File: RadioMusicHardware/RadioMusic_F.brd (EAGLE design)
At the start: 107 x 19 mm, 31 parts, among them X1 VERT_SD_CARD

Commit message: Fixed issues on Rev1 proto boards
Diodes changed to BAT42
LED resistors changed to 2k
Ground error on Front board fixed
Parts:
- D7, D8: value BAT81 -> BAT42
- R11, R12, R13, R14, R15: value 1k -> 2K
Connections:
- removed net GND: R10.1, R21.1
- net GND_F: now also R10.1, R21.1
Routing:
- net GND: track 5.93 -> 0.00 mm
- net GND_F: track 172.3 -> 174.2 mm
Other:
- board text added: "<-BAT42 x2"
- board text removed: "<-BAT81 x2"
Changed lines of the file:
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@@
 <text x="70.485" y="11.43" size="1.27" layer="22" rot="MR90">--&gt;</text>
 <text x="71.755" y="6.985" size="1.27" layer="22" rot="SMR270">--&gt;</text>
-<text x="36.3474" y="13.9192" size="0.762" layer="21" rot="R90" align="center-left">&lt;-BAT81
+<text x="36.3474" y="13.9192" size="0.762" layer="21" rot="R90" align="center-left">&lt;-BAT42
    x2</text>
 <text x="74.0664" y="0.7112" size="0.762" layer="21" distance="40">Be super careful with
@@
 <element name="R20" library="TomW" package="0207/10" value="100k" x="76.835" y="9.525" rot="R90"/>
 <element name="R21" library="TomW" package="0207/10" value="200k" x="79.375" y="9.525" rot="R90"/>
-<element name="D7" library="diode" package="DO34-7" value="BAT81" x="36.83" y="9.525" smashed="yes" rot="R90"/>
-<element name="D8" library="diode" package="DO34-7" value="BAT81" x="34.925" y="9.525" smashed="yes" rot="R270"/>
+<element name="D7" library="diode" package="DO34-7" value="BAT42" x="36.83" y="9.525" smashed="yes" rot="R90"/>
+<element name="D8" library="diode" package="DO34-7" value="BAT42" x="34.925" y="9.525" smashed="yes" rot="R270"/>
 <element name="R19" library="TomW" package="0207/10" value="100k" x="32.385" y="9.525" rot="R90"/>
 <element name="R18" library="TomW" package="0207/10" value="220R" x="29.845" y="9.525" rot="R90"/>
@@
 <element name="LED3" library="TomW" package="LED3MM" value="" x="105.156" y="7.366" rot="R270"/>
 <element name="LED4" library="TomW" package="LED3MM" value="" x="105.156" y="2.921" rot="R270"/>
-<element name="R11" library="TomW" package="0207/10" value="1k" x="97.155" y="17.145"/>
-<element name="R12" library="TomW" package="0207/10" value="1k" x="102.235" y="9.525" rot="R90"/>
-<element name="R13" library="TomW" package="0207/10" value="1k" x="81.915" y="9.525" rot="R90"/>
-<element name="R14" library="TomW" package="0207/10" value="1k" x="95.885" y="1.905"/>
+<element name="R11" library="TomW" package="0207/10" value="2K" x="97.155" y="17.145"/>
+<element name="R12" library="TomW" package="0207/10" value="2K" x="102.235" y="9.525" rot="R90"/>
+<element name="R13" library="TomW" package="0207/10" value="2K" x="81.915" y="9.525" rot="R90"/>
+<element name="R14" library="TomW" package="0207/10" value="2K" x="95.885" y="1.905"/>
 <element name="X1" library="TomW" package="VERT_MICROSD" value="VERT_SD_CARD" x="44.45" y="16.51"/>
 <element name="LED5" library="TomW" package="LED3MM" value="" x="52.705" y="3.175" smashed="yes" rot="R270">
 <attribute name="VALUE" x="51.054" y="1.27" size="1.27" layer="51" ratio="10" rot="R270"/>
 </element>
-<element name="R15" library="TomW" package="0207/10" value="1k" x="55.245" y="9.525" rot="R90"/>
+<element name="R15" library="TomW" package="0207/10" value="2K" x="55.245" y="9.525" rot="R90"/>
 <element name="JP2" library="SparkFun-Connectors" package="1X11_LOCK" value="M11LOCK" x="82.55" y="17.145" locked="yes" smashed="yes" rot="MR0"/>
 <element name="JP4" library="SparkFun-Connectors" package="1X07_LOCK" value="" x="57.15" y="1.27" locked="yes" smashed="yes" rot="MR180">
@@
 </elements>
 <signals>
-<signal name="GND" class="2" airwireshidden="yes">
-<contactref element="R10" pad="1"/>
-<contactref element="R21" pad="1"/>
-<wire x1="80.4672" y1="5.4864" x2="79.4512" y2="4.4704" width="0.4572" layer="1"/>
-<wire x1="83.312" y1="5.4864" x2="80.4672" y2="5.4864" width="0.4572" layer="1"/>
-<wire x1="84.328" y1="4.4704" x2="83.312" y2="5.4864" width="0.4572" layer="1"/>
-<wire x1="79.4512" y1="4.4704" x2="79.375" y2="4.445" width="0.4572" layer="1"/>
-<wire x1="84.328" y1="4.4704" x2="84.455" y2="4.445" width="0.4572" layer="1"/>
-</signal>
 <signal name="VBAT">
 </signal>
@@
 <wire x1="88.1888" y1="6.9088" x2="88.25" y2="7.025" width="0.3048" layer="16"/>
 </signal>
-<signal name="GND_F" class="2" airwireshidden="yes">
+<signal name="GND_F" class="2">
 <contactref element="X1" pad="P$6"/>
 <contactref element="X1" pad="GND1"/>
@@
 <wire x1="40.0304" y1="13.208" x2="40.15" y2="13.34" width="0.4572" layer="16"/>
 <wire x1="34.9504" y1="5.8928" x2="34.925" y2="5.715" width="0.4572" layer="16"/>
-<wire x1="89.2048" y1="3.4544" x2="89.7128" y2="2.9464" width="0.4572" layer="1"/>
-<wire x1="89.7128" y1="2.9464" x2="90.6272" y2="2.032" width="0.4572" layer="1"/>
-<wire x1="82.9056" y1="3.4544" x2="89.2048" y2="3.4544" width="0.4572" layer="1"/>
-<wire x1="81.915" y1="4.445" x2="82.9056" y2="3.4544" width="0.4572" layer="1"/>
-<wire x1="90.6272" y1="2.032" x2="90.805" y2="1.905" width="0.4572" layer="1"/>
 <wire x1="100.9904" y1="3.048" x2="102.2096" y2="4.2672" width="0.4572" layer="1"/>
-<wire x1="89.8144" y1="3.048" x2="100.9904" y2="3.048" width="0.4572" layer="1"/>
 <wire x1="102.2096" y1="4.2672" x2="102.235" y2="4.445" width="0.4572" layer="1"/>
-<wire x1="89.8144" y1="3.048" x2="89.7128" y2="2.9464" width="0.4572" layer="1"/>
 <wire x1="88.392" y1="13.4112" x2="89.5096" y2="14.5288" width="0.4572" layer="16"/>
 <wire x1="89.5096" y1="14.5288" x2="92.0496" y2="17.0688" width="0.4572" layer="16"/>
@@
 <wire x1="60.1472" y1="12.192" x2="60.31" y2="12.025" width="0.4572" layer="1"/>
 <via x="57.5056" y="12.192" extent="1-16" drill="0.3048"/>
+<contactref element="R10" pad="1"/>
+<contactref element="R21" pad="1"/>
+<wire x1="100.9904" y1="3.048" x2="91.948" y2="3.048" width="0.4572" layer="1"/>
+<wire x1="91.948" y1="3.048" x2="90.805" y2="1.905" width="0.4572" layer="1"/>
+<wire x1="79.375" y1="4.445" x2="81.915" y2="4.445" width="0.4572" layer="1"/>
+<wire x1="81.915" y1="4.445" x2="84.455" y2="4.445" width="0.4572" layer="1"/>
+<wire x1="84.455" y1="4.445" x2="88.265" y2="4.445" width="0.4572" layer="1"/>
+<wire x1="88.265" y1="4.445" x2="90.805" y2="1.905" width="0.4572" layer="1"/>
 </signal>
 <signal name="CHANNEL_CV_F">

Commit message: Change resistor values to reduce CV noise
Fixes #13
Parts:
- R10, R21: value 200k -> 47k
- R11, R12, R13, R14, R15: value 2K -> 1.5k
- R20, R9: value 100k -> 22k
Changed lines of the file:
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@@
 <attribute name="NAME" x="6.35" y="1.3208" size="1.016" layer="21" rot="R180"/>
 </element>
-<element name="R9" library="TomW" package="0207/10" value="100k" x="57.785" y="9.525" rot="R90"/>
-<element name="R10" library="TomW" package="0207/10" value="200k" x="84.455" y="9.525" rot="R90"/>
+<element name="R9" library="TomW" package="0207/10" value="22k" x="57.785" y="9.525" rot="R90"/>
+<element name="R10" library="TomW" package="0207/10" value="47k" x="84.455" y="9.525" rot="R90"/>
 <element name="R17" library="TomW" package="0207/10" value="220R" x="74.295" y="9.525" rot="R90"/>
 <element name="TIME-POT" library="TomW" package="EVUF" value="50k" x="67.31" y="9.525" smashed="yes" rot="R270">
@@
 <attribute name="NAME" x="21.3614" y="11.2776" size="1.016" layer="21" rot="R180"/>
 </element>
-<element name="R20" library="TomW" package="0207/10" value="100k" x="76.835" y="9.525" rot="R90"/>
-<element name="R21" library="TomW" package="0207/10" value="200k" x="79.375" y="9.525" rot="R90"/>
+<element name="R20" library="TomW" package="0207/10" value="22k" x="76.835" y="9.525" rot="R90"/>
+<element name="R21" library="TomW" package="0207/10" value="47k" x="79.375" y="9.525" rot="R90"/>
 <element name="D7" library="diode" package="DO34-7" value="BAT42" x="36.83" y="9.525" smashed="yes" rot="R90"/>
 <element name="D8" library="diode" package="DO34-7" value="BAT42" x="34.925" y="9.525" smashed="yes" rot="R270"/>
@@
 <element name="LED3" library="TomW" package="LED3MM" value="" x="105.156" y="7.366" rot="R270"/>
 <element name="LED4" library="TomW" package="LED3MM" value="" x="105.156" y="2.921" rot="R270"/>
-<element name="R11" library="TomW" package="0207/10" value="2K" x="97.155" y="17.145"/>
-<element name="R12" library="TomW" package="0207/10" value="2K" x="102.235" y="9.525" rot="R90"/>
-<element name="R13" library="TomW" package="0207/10" value="2K" x="81.915" y="9.525" rot="R90"/>
-<element name="R14" library="TomW" package="0207/10" value="2K" x="95.885" y="1.905"/>
+<element name="R11" library="TomW" package="0207/10" value="1.5k" x="97.155" y="17.145"/>
+<element name="R12" library="TomW" package="0207/10" value="1.5k" x="102.235" y="9.525" rot="R90"/>
+<element name="R13" library="TomW" package="0207/10" value="1.5k" x="81.915" y="9.525" rot="R90"/>
+<element name="R14" library="TomW" package="0207/10" value="1.5k" x="95.885" y="1.905"/>
 <element name="X1" library="TomW" package="VERT_MICROSD" value="VERT_SD_CARD" x="44.45" y="16.51"/>
 <element name="LED5" library="TomW" package="LED3MM" value="" x="52.705" y="3.175" smashed="yes" rot="R270">
 <attribute name="VALUE" x="51.054" y="1.27" size="1.27" layer="51" ratio="10" rot="R270"/>
 </element>
-<element name="R15" library="TomW" package="0207/10" value="2K" x="55.245" y="9.525" rot="R90"/>
+<element name="R15" library="TomW" package="0207/10" value="1.5k" x="55.245" y="9.525" rot="R90"/>
 <element name="JP2" library="SparkFun-Connectors" package="1X11_LOCK" value="M11LOCK" x="82.55" y="17.145" locked="yes" smashed="yes" rot="MR0"/>
 <element name="JP4" library="SparkFun-Connectors" package="1X07_LOCK" value="" x="57.15" y="1.27" locked="yes" smashed="yes" rot="MR180">

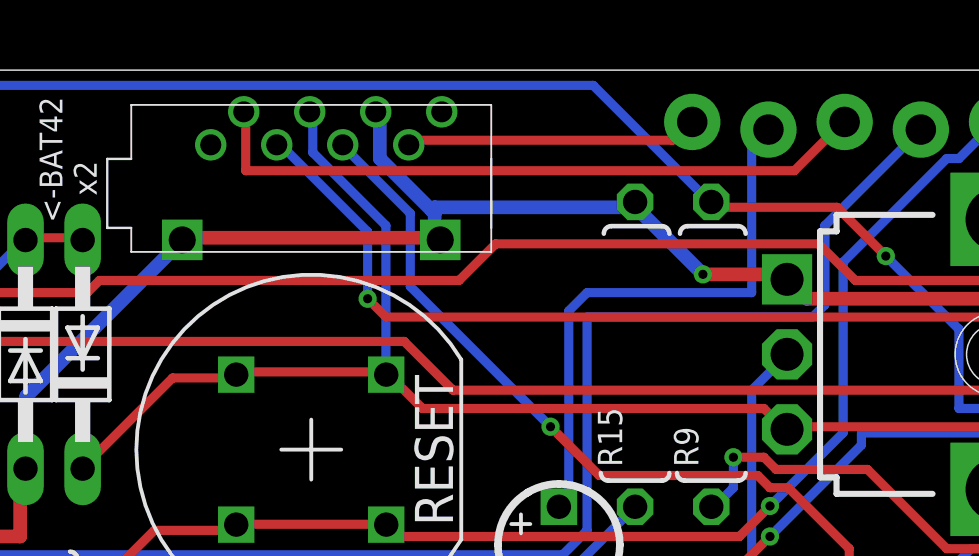
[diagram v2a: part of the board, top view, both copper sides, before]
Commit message: Fix SD Card pin position
Pin holes were 0.5mm off Fixes #14
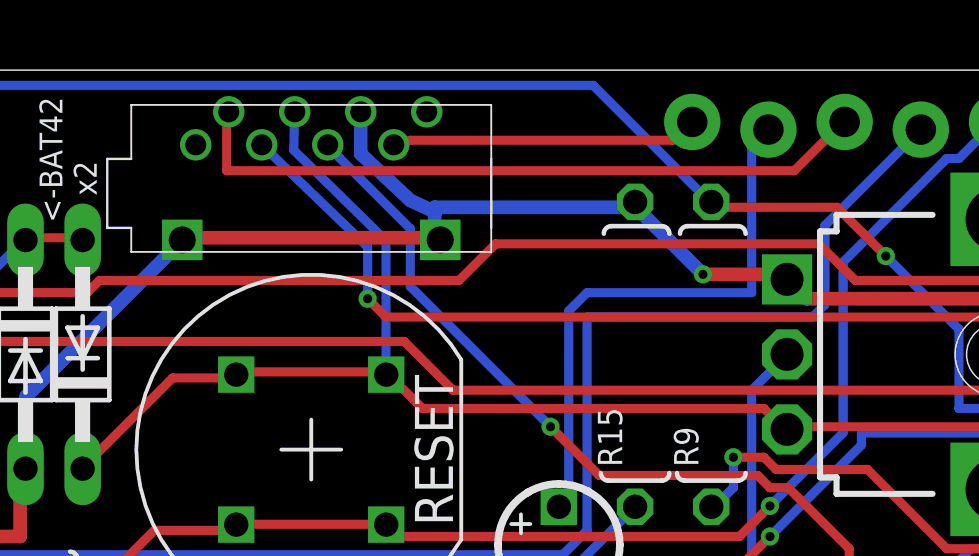
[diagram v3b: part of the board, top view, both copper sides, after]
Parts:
- X1: value VERT_SD_CARD -> VERT_SD_CARD_REV2; device TomW:VERT_MICROSD -> TomW:VERT_MICROSD_REV2
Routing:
- net SS_F: track 22.6 -> 23.3 mm
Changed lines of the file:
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@@
 <setting verticaltext="up"/>
 </settings>
-<grid distance="25" unitdist="mil" unit="mil" style="lines" multiple="1" display="yes" altdistance="8" altunitdist="mil" altunit="mil"/>
+<grid distance="25" unitdist="mil" unit="mil" style="lines" multiple="1" display="yes" altdistance="5" altunitdist="mil" altunit="mil"/>
 <layers>
 <layer number="1" name="Top" color="4" fill="1" visible="yes" active="yes"/>
@@
 <element name="R13" library="TomW" package="0207/10" value="1.5k" x="81.915" y="9.525" rot="R90"/>
 <element name="R14" library="TomW" package="0207/10" value="1.5k" x="95.885" y="1.905"/>
-<element name="X1" library="TomW" package="VERT_MICROSD" value="VERT_SD_CARD" x="44.45" y="16.51"/>
+<element name="X1" library="TomW" package="VERT_MICROSD_REV2" value="VERT_SD_CARD_REV2" x="44.45" y="16.51"/>
 <element name="LED5" library="TomW" package="LED3MM" value="" x="52.705" y="3.175" smashed="yes" rot="R270">
 <attribute name="VALUE" x="51.054" y="1.27" size="1.27" layer="51" ratio="10" rot="R270"/>
@@
 <wire x1="56.4896" y1="16.6624" x2="47.752" y2="16.6624" width="0.3048" layer="1"/>
 <wire x1="57.0992" y1="17.272" x2="56.4896" y2="16.6624" width="0.3048" layer="1"/>
-<wire x1="47.752" y1="16.6624" x2="47.7" y2="16.51" width="0.3048" layer="1"/>
+<wire x1="47.752" y1="16.6624" x2="47.2" y2="16.51" width="0.3048" layer="1"/>
 <wire x1="57.0992" y1="17.272" x2="57.15" y2="17.272" width="0.3048" layer="1"/>
 </signal>
@@
 <contactref element="RESET" pad="P$4"/>
 <contactref element="JP4" pad="4"/>
-<wire x1="44.5008" y1="16.256" x2="44.5008" y2="17.4752" width="0.3048" layer="16"/>
-<wire x1="46.9392" y1="13.8176" x2="44.5008" y2="16.256" width="0.3048" layer="16"/>
-<wire x1="46.9392" y1="8.9408" x2="46.9392" y2="13.8176" width="0.3048" layer="16"/>
-<wire x1="44.5008" y1="17.4752" x2="44.4" y2="17.61" width="0.3048" layer="16"/>
+<wire x1="46.5328" y1="13.716" x2="43.8658" y2="16.3322" width="0.3048" layer="16"/>
+<wire x1="46.9392" y1="13.3096" x2="46.5328" y2="13.716" width="0.3048" layer="16"/>
+<wire x1="46.9392" y1="8.9408" x2="46.9392" y2="13.3096" width="0.3048" layer="16"/>
+<wire x1="43.8658" y1="16.3322" x2="43.9" y2="17.61" width="0.3048" layer="16"/>
 <wire x1="46.9392" y1="8.9408" x2="46.95" y2="8.85" width="0.3048" layer="16"/>
 <wire x1="46.9392" y1="8.9408" x2="42.0624" y2="8.9408" width="0.3048" layer="1"/>
@@
 <contactref element="R8" pad="1"/>
 <contactref element="JP2" pad="1"/>
-<wire x1="46.736" y1="16.0528" x2="46.736" y2="17.4752" width="0.4572" layer="16"/>
+<wire x1="47.752" y1="14.6558" x2="46.101" y2="16.2052" width="0.4572" layer="16"/>
 <wire x1="48.5648" y1="14.224" x2="48.4632" y2="14.3256" width="0.4572" layer="16"/>
-<wire x1="48.4632" y1="14.3256" x2="46.736" y2="16.0528" width="0.4572" layer="16"/>
+<wire x1="48.4632" y1="14.3256" x2="47.752" y2="14.6558" width="0.4572" layer="16"/>
 <wire x1="48.5648" y1="13.4112" x2="48.5648" y2="14.224" width="0.4572" layer="16"/>
-<wire x1="46.736" y1="17.4752" x2="46.6" y2="17.61" width="0.4572" layer="16"/>
+<wire x1="46.101" y1="16.2052" x2="46.1" y2="17.61" width="0.4572" layer="16"/>
 <wire x1="48.5648" y1="13.4112" x2="48.75" y2="13.34" width="0.4572" layer="16"/>
 <wire x1="48.5648" y1="14.4272" x2="55.0672" y2="14.4272" width="0.4572" layer="16"/>
@@
 <contactref element="X1" pad="P$5"/>
 <contactref element="JP4" pad="3"/>
-<wire x1="47.752" y1="14.224" x2="45.5168" y2="16.4592" width="0.3048" layer="16"/>
-<wire x1="47.752" y1="11.7856" x2="47.752" y2="14.224" width="0.3048" layer="16"/>
+<wire x1="47.752" y1="13.716" x2="45.3898" y2="16.0782" width="0.3048" layer="16"/>
+<wire x1="47.752" y1="11.7856" x2="47.752" y2="13.716" width="0.3048" layer="16"/>
 <wire x1="52.4256" y1="7.112" x2="47.752" y2="11.7856" width="0.3048" layer="16"/>
 <wire x1="54.0512" y1="5.4864" x2="52.4256" y2="7.112" width="0.3048" layer="1"/>
@@
 <wire x1="62.3824" y1="3.048" x2="60.3504" y2="5.08" width="0.3048" layer="1"/>
 <wire x1="62.3824" y1="1.2192" x2="62.3824" y2="3.048" width="0.3048" layer="1"/>
-<wire x1="45.5168" y1="16.4592" x2="45.5" y2="16.51" width="0.3048" layer="16"/>
+<wire x1="45.3898" y1="16.0782" x2="45" y2="16.51" width="0.3048" layer="16"/>
 <wire x1="62.3824" y1="1.2192" x2="62.23" y2="1.143" width="0.3048" layer="1"/>
 <via x="52.4256" y="7.112" extent="1-16" drill="0.3048"/>
@@
 <contactref element="X1" pad="P$3"/>
 <contactref element="JP2" pad="6"/>
-<wire x1="46.3296" y1="13.6144" x2="43.4848" y2="16.4592" width="0.3048" layer="16"/>
-<wire x1="46.3296" y1="11.3792" x2="46.3296" y2="13.6144" width="0.3048" layer="16"/>
+<wire x1="46.3296" y1="13.1064" x2="42.8498" y2="16.4592" width="0.3048" layer="16"/>
+<wire x1="46.3296" y1="11.3792" x2="46.3296" y2="13.1064" width="0.3048" layer="16"/>
 <wire x1="46.9392" y1="10.7696" x2="46.3296" y2="11.3792" width="0.3048" layer="1"/>
 <wire x1="67.2592" y1="10.7696" x2="46.9392" y2="10.7696" width="0.3048" layer="1"/>
@@
 <wire x1="69.6976" y1="12.8016" x2="67.4624" y2="10.5664" width="0.3048" layer="16"/>
 <wire x1="69.6976" y1="16.8656" x2="69.6976" y2="12.8016" width="0.3048" layer="16"/>
-<wire x1="43.4848" y1="16.4592" x2="43.3" y2="16.51" width="0.3048" layer="16"/>
+<wire x1="42.8498" y1="16.4592" x2="42.8" y2="16.51" width="0.3048" layer="16"/>
 <wire x1="69.6976" y1="16.8656" x2="69.85" y2="17.018" width="0.3048" layer="16"/>
 <via x="46.3296" y="11.3792" extent="1-16" drill="0.3048"/>
@@
 <contactref element="X1" pad="P$2"/>
 <contactref element="JP2" pad="9"/>
-<wire x1="42.2656" y1="15.6464" x2="42.2656" y2="17.4752" width="0.3048" layer="1"/>
-<wire x1="60.5536" y1="15.6464" x2="42.2656" y2="15.6464" width="0.3048" layer="1"/>
+<wire x1="41.6306" y1="15.6464" x2="41.6306" y2="17.4752" width="0.3048" layer="1"/>
+<wire x1="60.5536" y1="15.6464" x2="41.6306" y2="15.6464" width="0.3048" layer="1"/>
 <wire x1="62.1792" y1="17.272" x2="60.5536" y2="15.6464" width="0.3048" layer="1"/>
-<wire x1="42.2656" y1="17.4752" x2="42.2" y2="17.61" width="0.3048" layer="1"/>
+<wire x1="41.6306" y1="17.4752" x2="41.7" y2="17.61" width="0.3048" layer="1"/>
 <wire x1="62.1792" y1="17.272" x2="62.23" y2="17.272" width="0.3048" layer="1"/>
 </signal>

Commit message: Front PCB Cosmetics
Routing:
- net N$9: track 90.7 -> 84.0 mm
- net RESET_CV_F: track 60.0 -> 57.1 mm
- net LED2_F: track 38.2 -> 35.9 mm
- net +3.3V_F: track 91.8 -> 89.7 mm
- net GND_F: track 174.5 -> 172.9 mm
- net N$20: track 30.6 -> 29.5 mm
- net CHANNEL_CV_F: track 29.0 -> 28.2 mm
- net LED4_F: track 41.4 -> 40.8 mm
- net SS_F: track 23.3 -> 22.7 mm
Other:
- board text added: "Careful with LED Polarity->"
- board text removed: "Be super careful with LED Polarity up here -->"
